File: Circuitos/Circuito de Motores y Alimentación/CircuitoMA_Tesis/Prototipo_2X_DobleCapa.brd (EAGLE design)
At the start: 75 x 86 mm, 29 parts, among them Q1 IRLZ44Z, Q2 IRLZ44Z, Q3 IRLZ44Z, Q4 IRLZ44Z, X1 22-23-2021

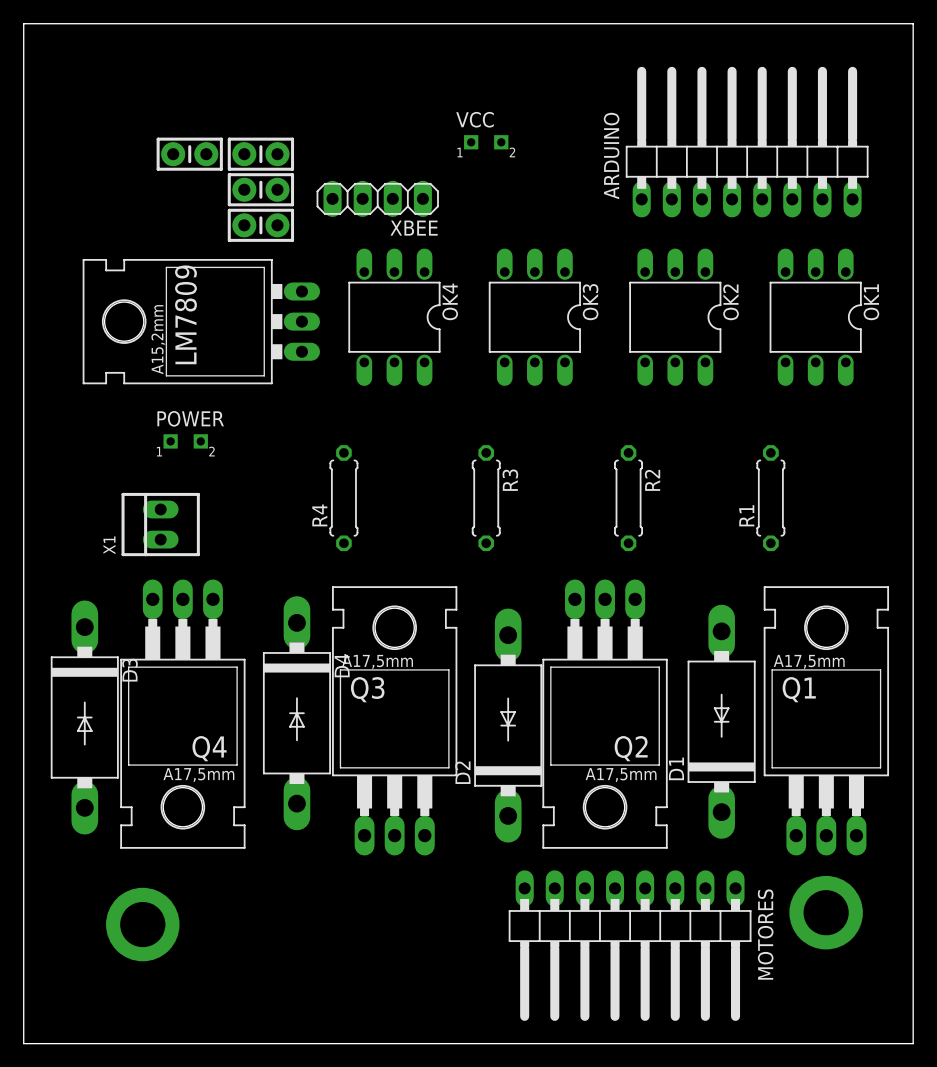
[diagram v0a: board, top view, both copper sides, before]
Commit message: Circuito
Circuito de motores y alimentación doble capa
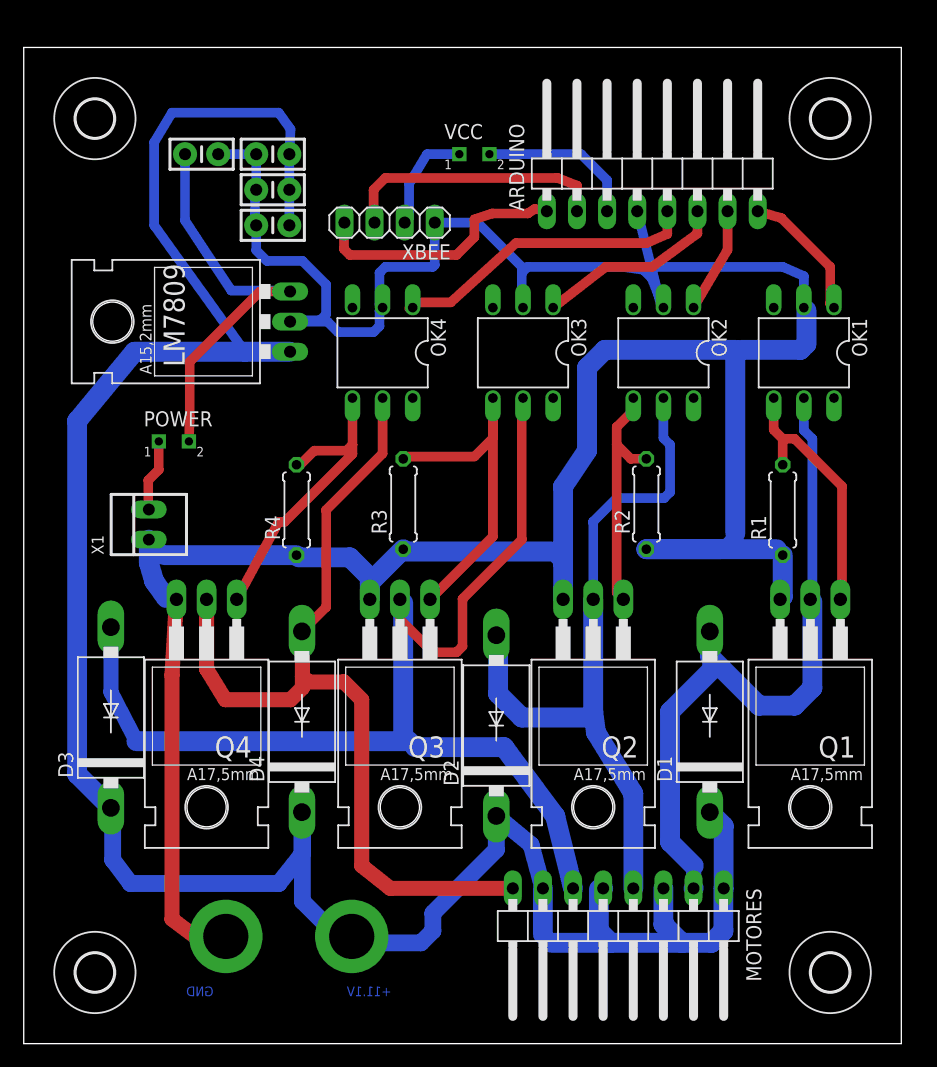
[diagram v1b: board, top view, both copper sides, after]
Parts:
- added H1, H2, H3, H4: MOUNT-HOLE3.2, holes:3,2
- moved +11,1V__BATERIA 40.0 mm to (27.7, 9.04)
- moved ARDUINO 8.06 mm to (53.0, 74.0)
- moved Q1 7.35 mm to (66.3, 31.1), turned to 180 degrees
- moved Q3 7.23 mm to (31.7, 31.1), turned to 180 degrees
- moved GND__BATERIA 7.07 mm to (17.0, 9.04)
- moved R3 7.02 mm to (32.0, 45.5), turned to 90 degrees
- moved R4 4.12 mm to (23.0, 45.0)
- moved OK1 3.16 mm to (65.8, 58.2)
- moved OK2 3.16 mm to (53.9, 58.2)
- moved OK3 3.16 mm to (42.1, 58.2)
- moved OK4 3.16 mm to (30.3, 58.2)
- moved XBEE 2.24 mm to (30.9, 69.2)
- moved D3 2.20 mm to (7.35, 27.5), turned to 90 degrees
- moved Q4 2.00 mm to (15.4, 31.1)
- moved R2 1.58 mm to (52.5, 45.5), turned to 90 degrees
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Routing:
- net GND: track 0.00 -> 258.8 mm
- net N$12: track 0.00 -> 203.3 mm
- net N$15: track 0.00 -> 98.5 mm
- net N$16: track 0.00 -> 76.3 mm
- net N$14: track 0.00 -> 62.6 mm
- net N$17: track 0.00 -> 61.9 mm
- net N$6: track 0.00 -> 35.3 mm
- net N$10: track 0.00 -> 30.8 mm
- net N$11: track 0.00 -> 26.2 mm
- net N$4: track 0.00 -> 26.0 mm
- net N$13: track 0.00 -> 22.7 mm
- net N$8: track 0.00 -> 22.2 mm
- net N$5: track 0.00 -> 21.9 mm
- net N$9: track 0.00 -> 20.8 mm
- net N$3: track 0.00 -> 16.2 mm
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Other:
- board size 75 x 86 mm -> 74 x 84 mm
- board text added: "+11.1V"
- board text added: "GND"
